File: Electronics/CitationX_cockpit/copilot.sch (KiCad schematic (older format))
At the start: 0 parts

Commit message: Electronics - Working on copilot side and APU
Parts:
- added C? (x5): 0.1u, symbol Device:C_Small
- added J? (x6): Screw_Terminal_01x10, symbol Connector:Screw_Terminal_01x10
- added J?: Screw_Terminal_01x02, symbol Connector:Screw_Terminal_01x02
- added R?: 1k, symbol Device:R
- added RN? (x4): R_Network08, Resistor_THT:R_Array_SIP9, symbol Device:R_Network08
- added U? (x4): 74HC165, symbol pkl_misc:74HC165
- added U?: 74HC595, symbol 74xx:74HC595
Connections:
- new net: U?.10 (SER), U?.9 (QH) (x3)
- new net: RN?.5 (R4), U?.3 (D4)
- new net: RN?.4 (R3), U?.4 (D5)
- new net: RN?.3 (R2), U?.5 (D6)
- new net: RN?.2 (R1), U?.6 (D7)
- new net: J?.10 (Pin_10), J?.6 (Pin_6), J?.7 (Pin_7), J?.8 (Pin_8), J?.9 (Pin_9), R?.1
- new net +3V3: C?.1, C?.1, C?.1, C?.1, C?.1, RN?.1 (common), RN?.1 (common), RN?.1 (common), RN?.1 (common), U?.10 (~SRCLR), U?.16 (VCC), U?.16 (VCC), U?.16 (VCC), U?.16 (VCC), U?.16 (VCC)
- new net ANTISKID: J?.1 (Pin_1), RN?.9 (R8), U?.11 (D0)
- new net AUX_PUMP: J?.8 (Pin_8), RN?.4 (R3), U?.4 (D5)
- new net CLK: U?.11 (SRCLK), U?.2 (CLK), U?.2 (CLK), U?.2 (CLK), U?.2 (CLK)
- new net ENGINE_LH: J?.3 (Pin_3), RN?.9 (R8), U?.11 (D0)
- new net ENGINE_RH: J?.4 (Pin_4), RN?.8 (R7), U?.12 (D1)
- new net GEARS: J?.1 (Pin_1), RN?.9 (R8), U?.11 (D0)
- new net GEARS_LH: J?.3 (Pin_3), U?.1 (QB)
- new net GEARS_LOCKED: J?.5 (Pin_5), U?.3 (QD)
- new net GEARS_NO: J?.2 (Pin_2), U?.15 (QA)
- new net GEARS_RH: J?.4 (Pin_4), U?.2 (QC)
- new net GND: C?.2, C?.2, C?.2, C?.2, C?.2, J?.1 (Pin_1), J?.1 (Pin_1), J?.1 (Pin_1), J?.10 (Pin_10), J?.10 (Pin_10), J?.2 (Pin_2), J?.2 (Pin_2), J?.2 (Pin_2), J?.3 (Pin_3), J?.3 (Pin_3), J?.3 (Pin_3), J?.4 (Pin_4), J?.4 (Pin_4), J?.4 (Pin_4), J?.5 (Pin_5), J?.5 (Pin_5), J?.5 (Pin_5), J?.6 (Pin_6), J?.6 (Pin_6), J?.7 (Pin_7), J?.7 (Pin_7), J?.8 (Pin_8), J?.8 (Pin_8), J?.9 (Pin_9), J?.9 (Pin_9), R?.2, U?.13 (~OE), U?.15 (CLK_INH), U?.15 (CLK_INH), U?.15 (CLK_INH), U?.15 (CLK_INH), U?.8 (GND), U?.8 (GND), U?.8 (GND), U?.8 (GND), U?.8 (GND)
- new net GND_REC_ANTICOLL: J?.2 (Pin_2), RN?.8 (R7), U?.12 (D1)
- new net GND_REC_OFF: J?.3 (Pin_3), RN?.7 (R6), U?.13 (D2)
- new net ISR_IN: U?.10 (SER)
- new net ISR_LATCH: U?.1 (SH/~LD), U?.1 (SH/~LD), U?.1 (SH/~LD), U?.1 (SH/~LD)
- new net ISR_OUT: U?.9 (QH)
- new net NAV: J?.7 (Pin_7), RN?.3 (R2), U?.5 (D6)
- new net OSR_IN: U?.14 (SER)
- new net OSR_LATCH: U?.12 (RCLK)
- new net OSR_OUT: U?.9 (QH')
- new net PAC_BLEED: J?.1 (Pin_1), RN?.7 (R6), U?.13 (D2)
- new net PILOT_LH: J?.6 (Pin_6), RN?.8 (R7), U?.12 (D1)
- new net PILOT_RH: J?.7 (Pin_7), RN?.7 (R6), U?.13 (D2)
- new net PRESS_ALT_SEL: J?.9 (Pin_9), RN?.9 (R8), U?.11 (D0)
- new net PRESS_MANUAL: J?.10 (Pin_10), RN?.8 (R7), U?.12 (D1)
- new net PUMP_A: J?.9 (Pin_9), RN?.3 (R2), U?.5 (D6)
- new net PUMP_B: J?.10 (Pin_10), RN?.2 (R1), U?.6 (D7)
- new net RECOG: J?.6 (Pin_6), RN?.4 (R3), U?.4 (D5)
- new net SB_PASS_SAFETY: J?.5 (Pin_5), RN?.5 (R4), U?.3 (D4)
- new net SEAT_BELTS_ON: J?.4 (Pin_4), RN?.6 (R5), U?.14 (D3)
- new net SLAT: J?.7 (Pin_7), RN?.5 (R4), U?.3 (D4)
- new net STAB_LH: J?.5 (Pin_5), RN?.7 (R6), U?.13 (D2)
- new net STAB_RH: J?.6 (Pin_6), RN?.6 (R5), U?.14 (D3)
- new net TAIL_FLOOD: J?.8 (Pin_8), RN?.2 (R1), U?.6 (D7)
- new net UNKN: J?.1 (Pin_1), RN?.3 (R2), U?.5 (D6)
- new net WEBMAC: J?.2 (Pin_2), RN?.6 (R5), U?.14 (D3)
- new net WIL: J?.8 (Pin_8), RN?.6 (R5), U?.14 (D3)
- new net WING_XOVER: J?.2 (Pin_2), RN?.2 (R1), U?.6 (D7)
- new net WSHLD_LH: J?.9 (Pin_9), RN?.5 (R4), U?.3 (D4)
- new net WSHLD_RH: J?.10 (Pin_10), RN?.4 (R3), U?.4 (D5)
- no-connect marks 0 -> 8
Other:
- note added: "8-channel output shift register"

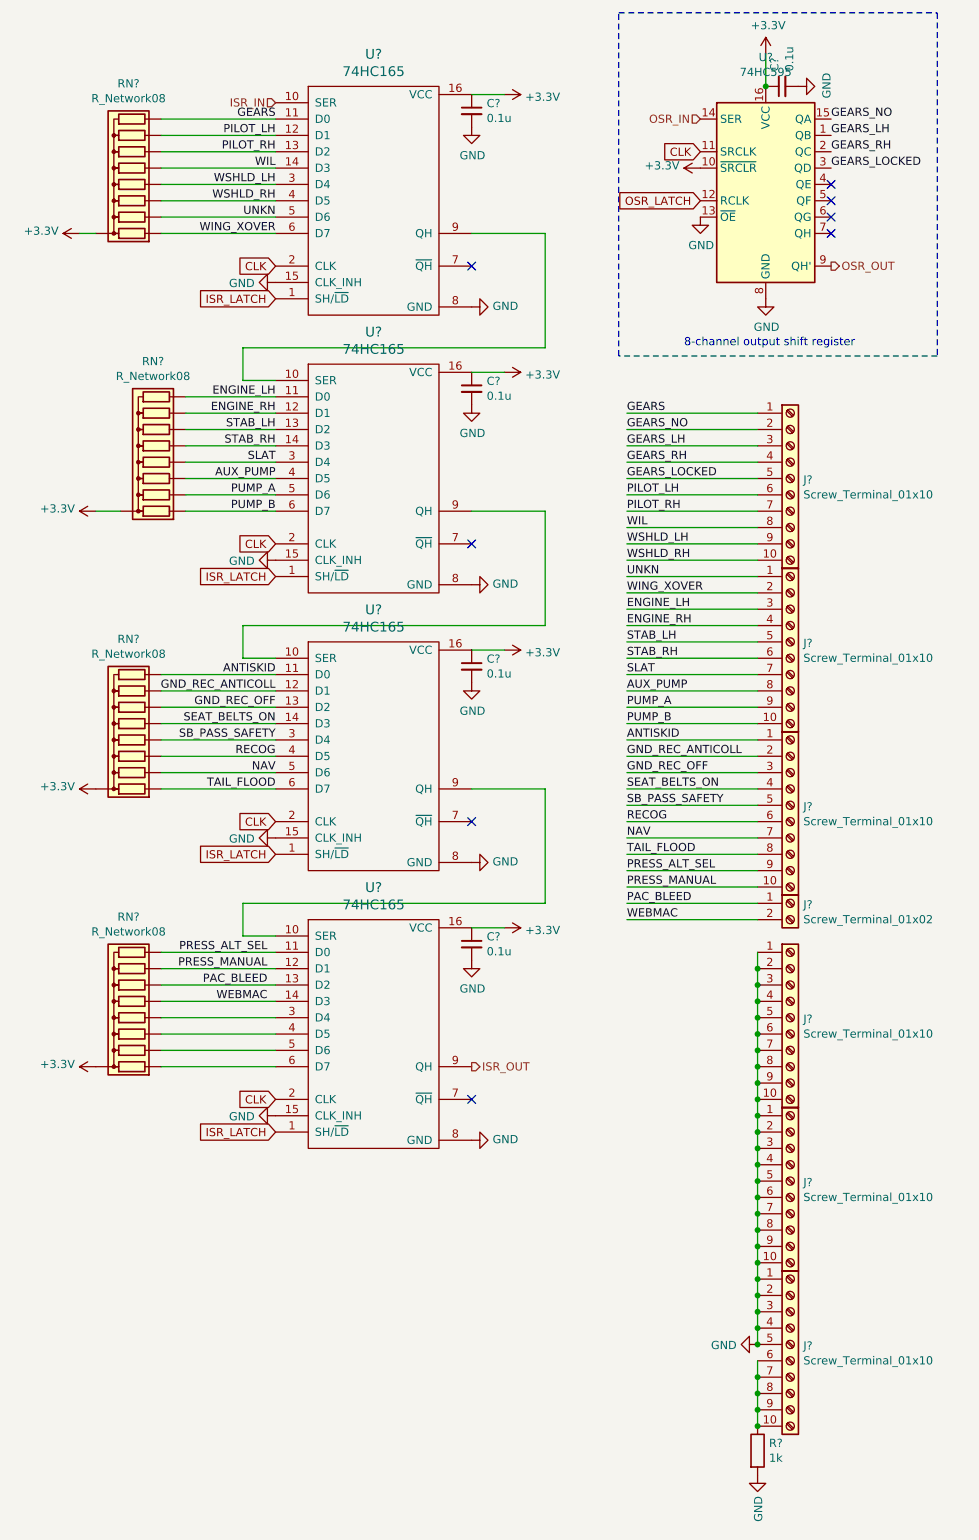
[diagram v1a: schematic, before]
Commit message: Electronics - Misc. works
Continued (and checked board). All connections are probably OK.
Fixed hierarchical pins in APUs (affects all schematics)
Numbered elements for testing schematics
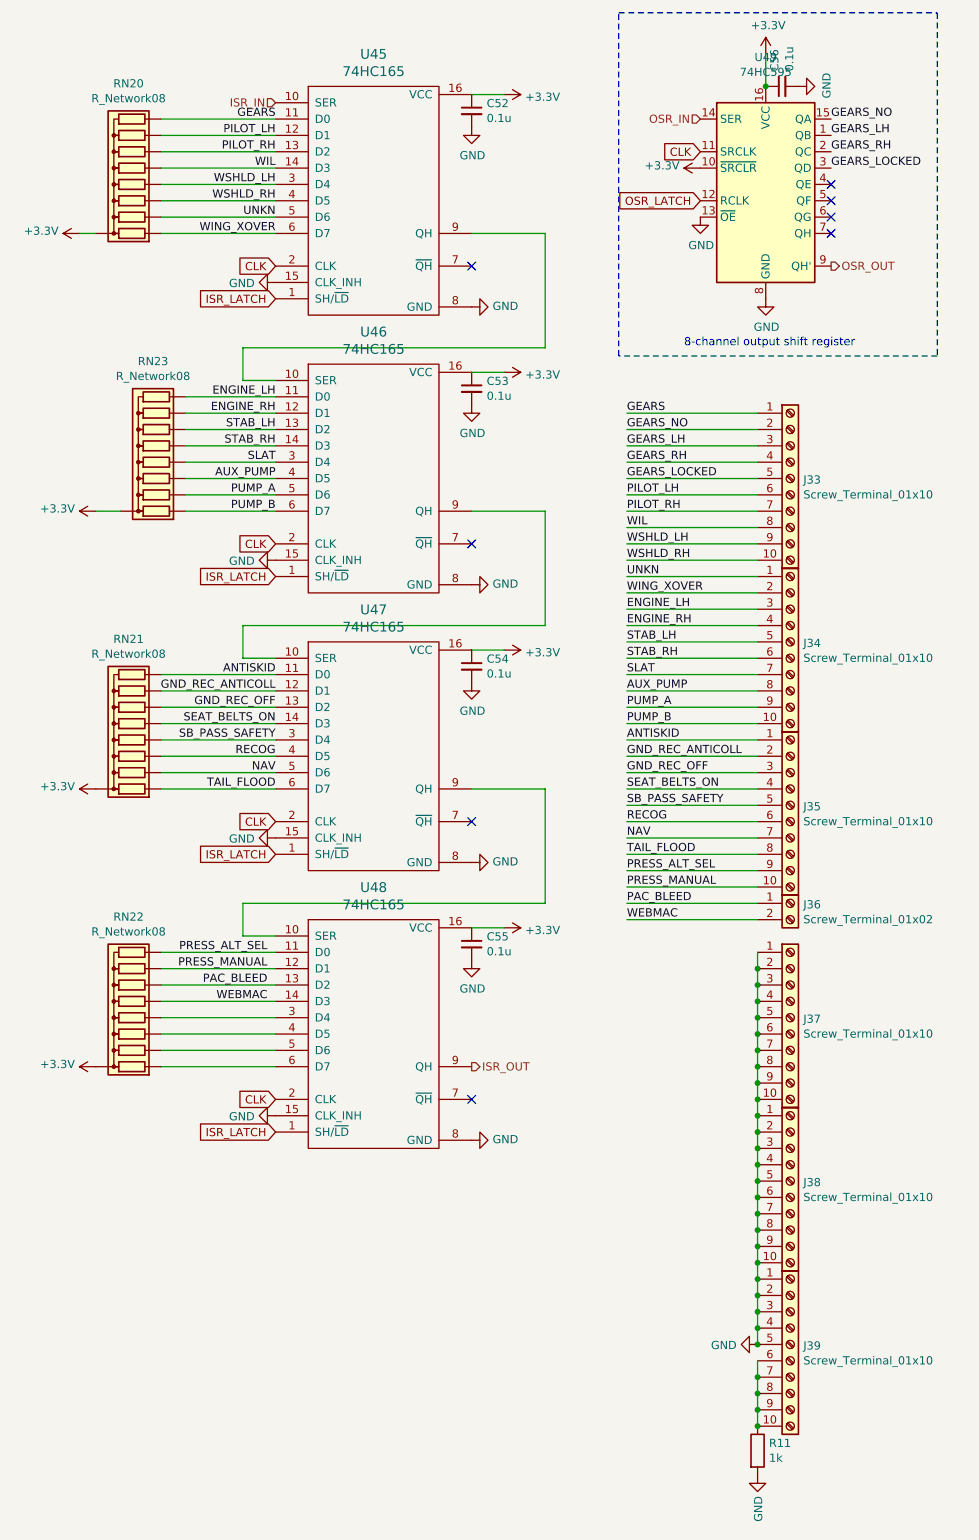
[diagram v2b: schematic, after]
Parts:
- gave numbers to parts that had none: 22

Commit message: Electronics - Misc works
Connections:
- net UNKN: no longer RN20.3 (R2), U45.5 (D6)
- new net WS_AIR: RN20.3 (R2), U45.5 (D6)
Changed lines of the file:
@@
 EESchema Schematic File Version 4
 LIBS:CitationX_cockpit-cache
-EELAYER 30 0
+EELAYER 26 0
 EELAYER END
 $Descr A3 11693 16535 portrait
@@
 WSHLD_RH
 Text Label 2500 2050 2    50   ~ 0
-UNKN
+WS_AIR
 Text Label 5900 1550 0    50   ~ 0
 GEARS_LH
